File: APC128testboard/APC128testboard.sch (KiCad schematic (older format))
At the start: 2 parts, among them P1 CONN_20X2

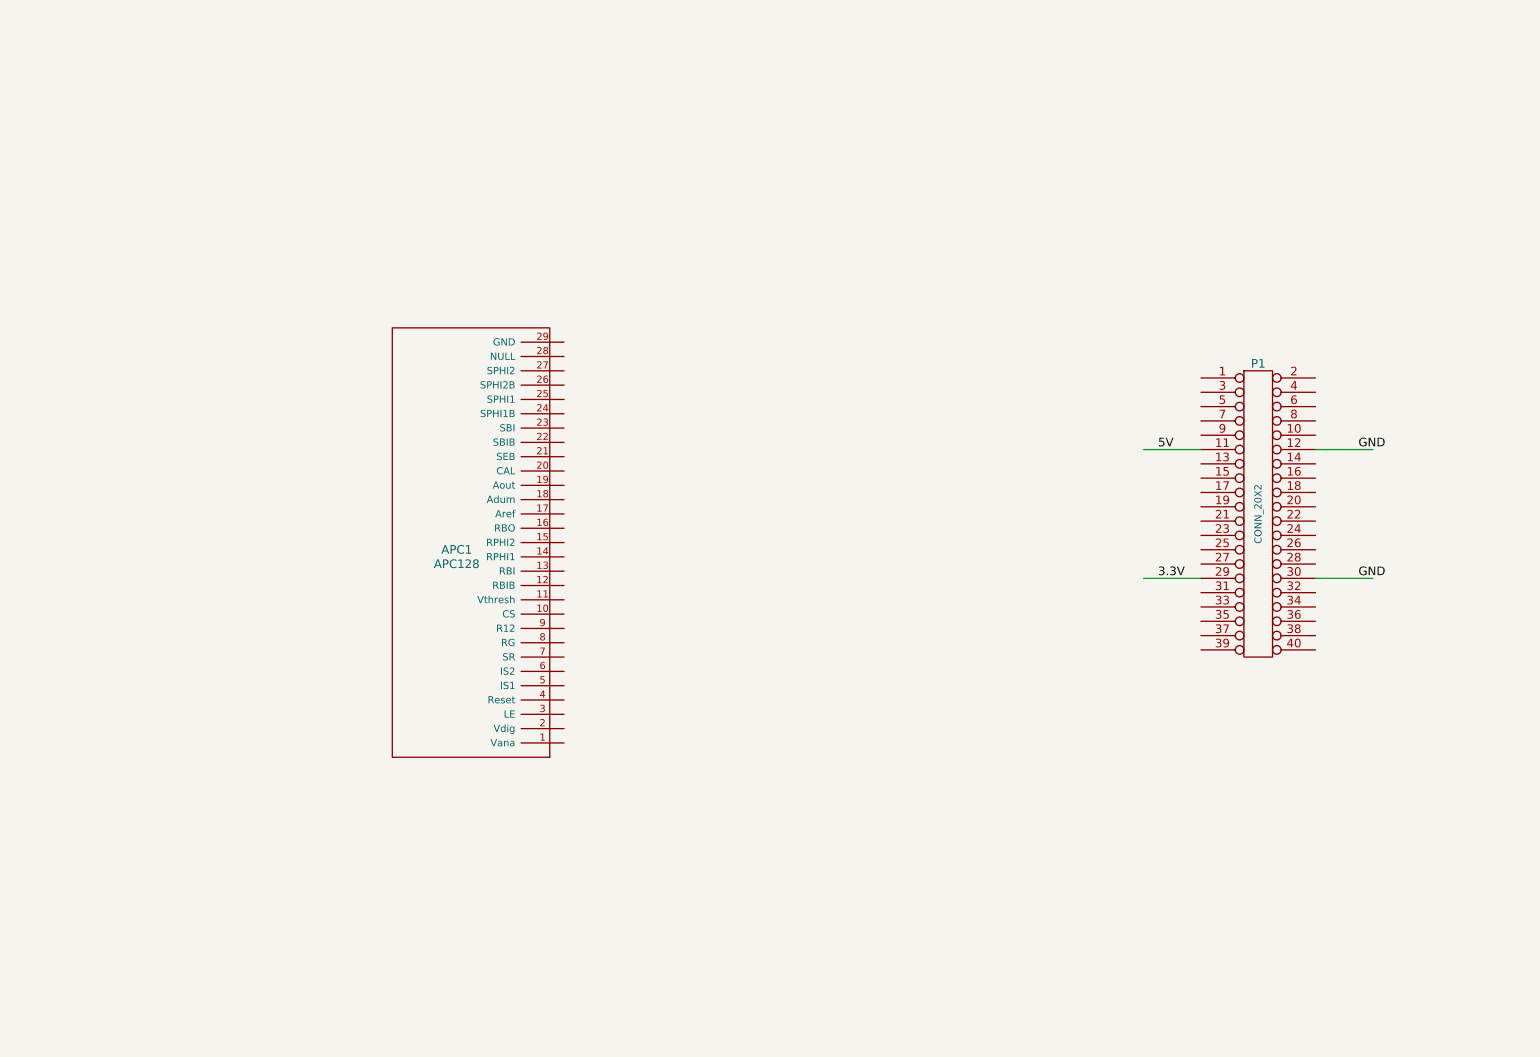
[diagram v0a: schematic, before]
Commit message: Moved existing Kicad files to legacy because they adhere to a depreciated version of Kicad. Added the APC128testboard project.
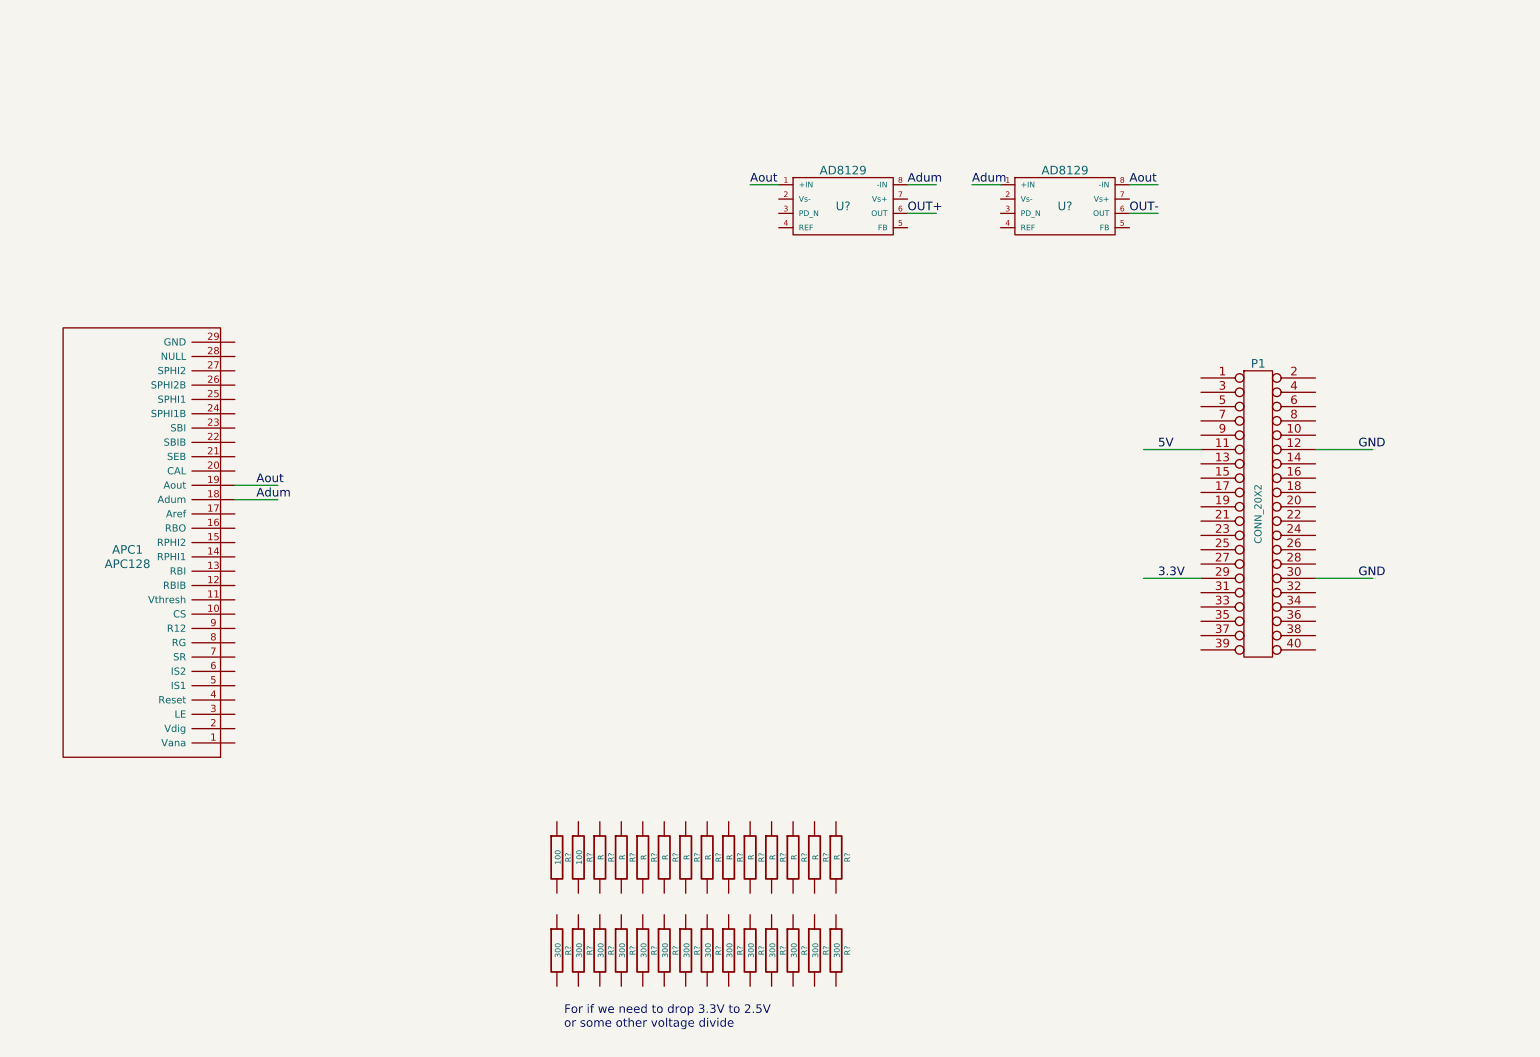
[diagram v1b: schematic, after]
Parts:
- added R? (x14): 300, symbol R
- added R? (x12): R, symbol R
- added R? (x2): 100, symbol R
- added U? (x2): AD8129, symbol AD8129
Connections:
- net labels added: Adum, Aout, OUT+, OUT-
- wire segments 4 -> 12
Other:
- note added: "For if we need to drop 3.3V to 2.5V \nor some other voltage divide"
- moved on the sheet: APC1

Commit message: Add DAC and pots to APC128testboard for adjustable analog inputs.
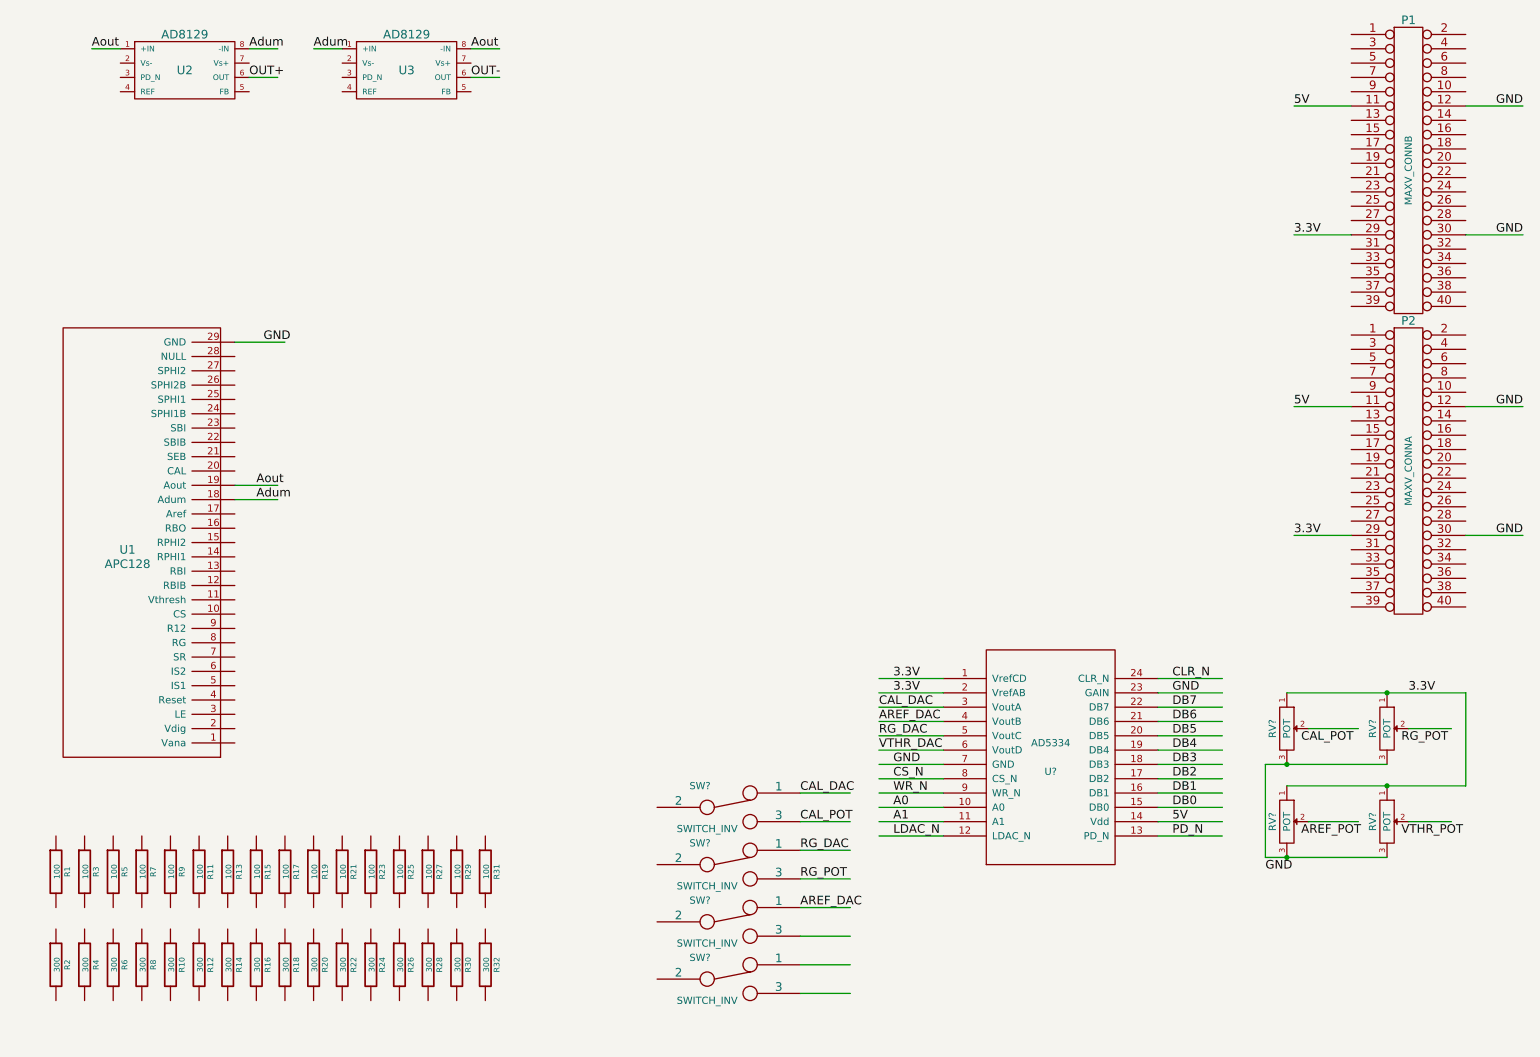
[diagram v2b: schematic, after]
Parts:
- removed R? (x13): 300, symbol R
- removed R? (x12): R, symbol R
- removed R?: 100, symbol R
- added P1: MAXV_CONNB, symbol CONN_20X2
- added R1, R11, R13, R15, R19, R21, R23, R25, R27, R29, R3, R31, R5, R7, R9: 100, symbol R
- added R10, R12, R14, R16, R2, R20, R22, R24, R26, R28, R30, R32, R4, R6, R8: 300, symbol R
- added RV? (x4): POT, symbol POT
- added SW? (x4): SWITCH_INV, symbol SWITCH_INV
- added U?: AD5334, MODULE, symbol AD5334
- P2: renamed from P1; value CONN_20X2 -> MAXV_CONNA
- gave numbers to parts that had none: 4
- renumbered APC1 to U1
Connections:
- net labels added: A0, A1, AREF_DAC, AREF_POT, CAL_DAC, CAL_POT, CLR_N, CS_N, DB0, DB1, DB2, DB3, DB4, DB5, DB6, DB7, LDAC_N, PD_N, RG_DAC, RG_POT, VTHR_DAC, VTHR_POT, WR_N
- wire segments 12 -> 59
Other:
- note removed: "For if we need to drop 3.3V to 2.5V \nor some other voltage divide"
- moved on the sheet: P2, R17, R18, U2, U3

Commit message: Continued progress on APC128Testboard.
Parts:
- R29, R31: value 100 -> R
- R30, R32: value 300 -> R
- gave numbers to parts that had none: 9
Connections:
- net labels added: AREF, CAL, CS, CS_d, IS1, IS1_d, IS2, IS2_d, LE, LE_d, R12, R12_d, RBI, RBI_d, RG, RPhi1, RPhi1_d, RPhi2, RPhi2_d, Reset, Reset_d, SBI, SBI_d, SEB, SEB_d, SPhi1, SPhi1_d, SPhi2, SPhi2_d, SR, SR_d, Sphi2_d, VTHR
- wire segments 59 -> 133
- no-connect marks 0 -> 5
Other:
- note added: "ConnA: 3.3V\nConnB: 2.5V"
- moved on the sheet: R10, R12, R14, R16, R18, R2, R20, R22, R24, R26, R28, R4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

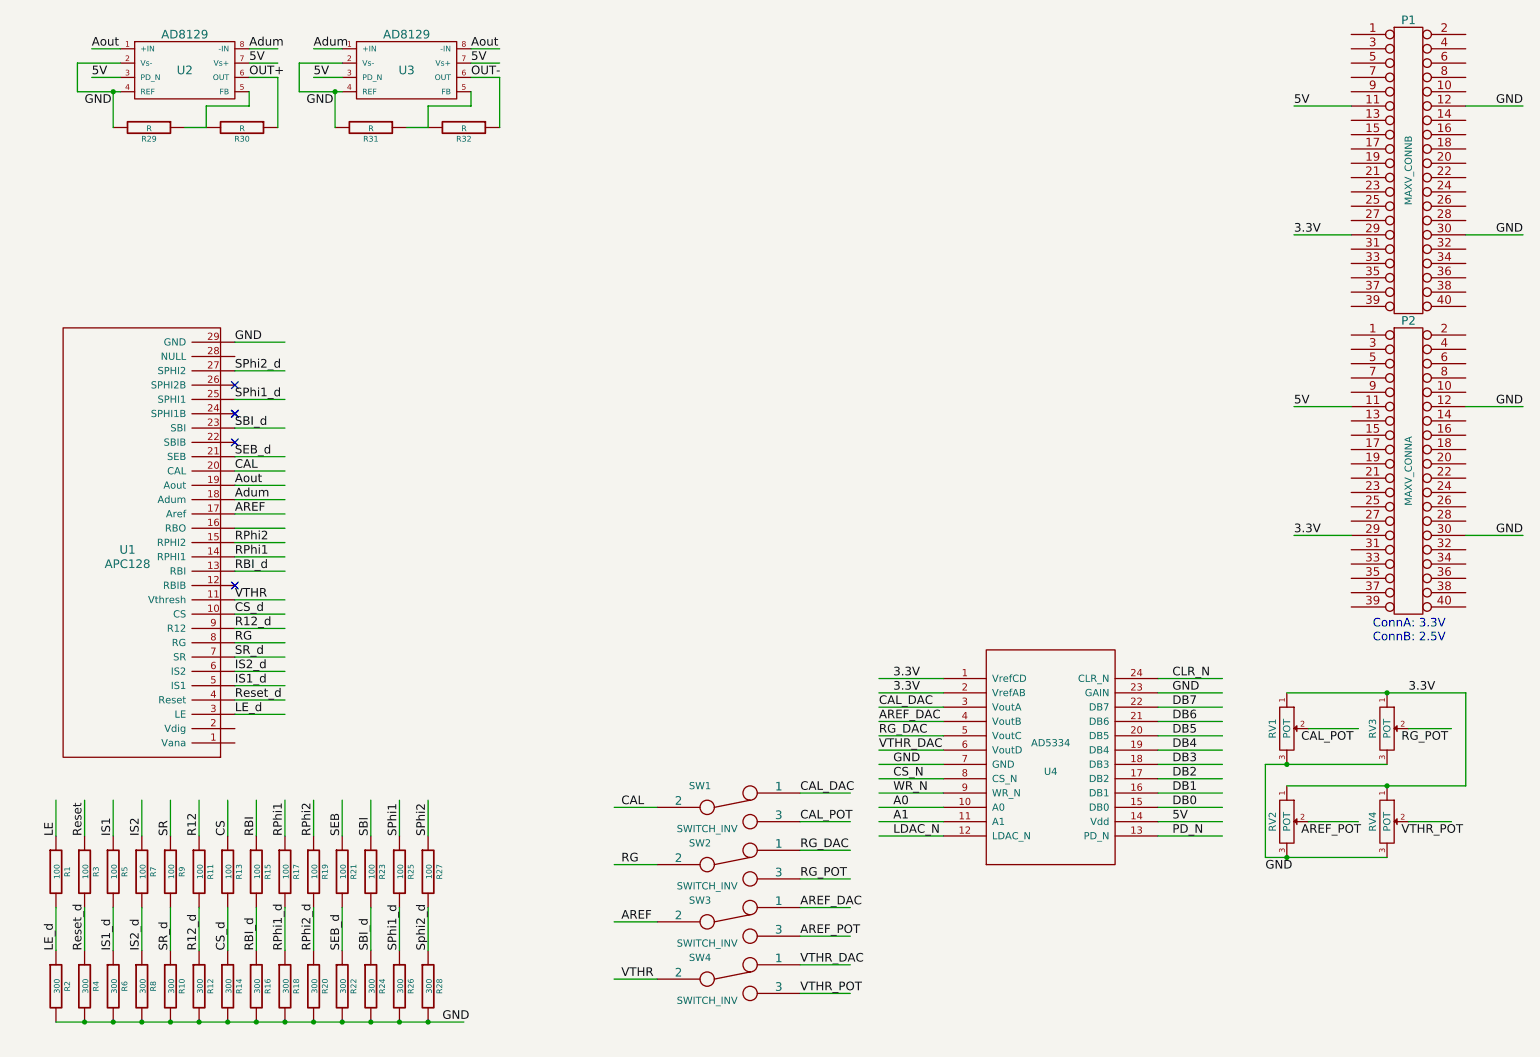
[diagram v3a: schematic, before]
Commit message: Finished first iteration of APC128Testboard circuit design.
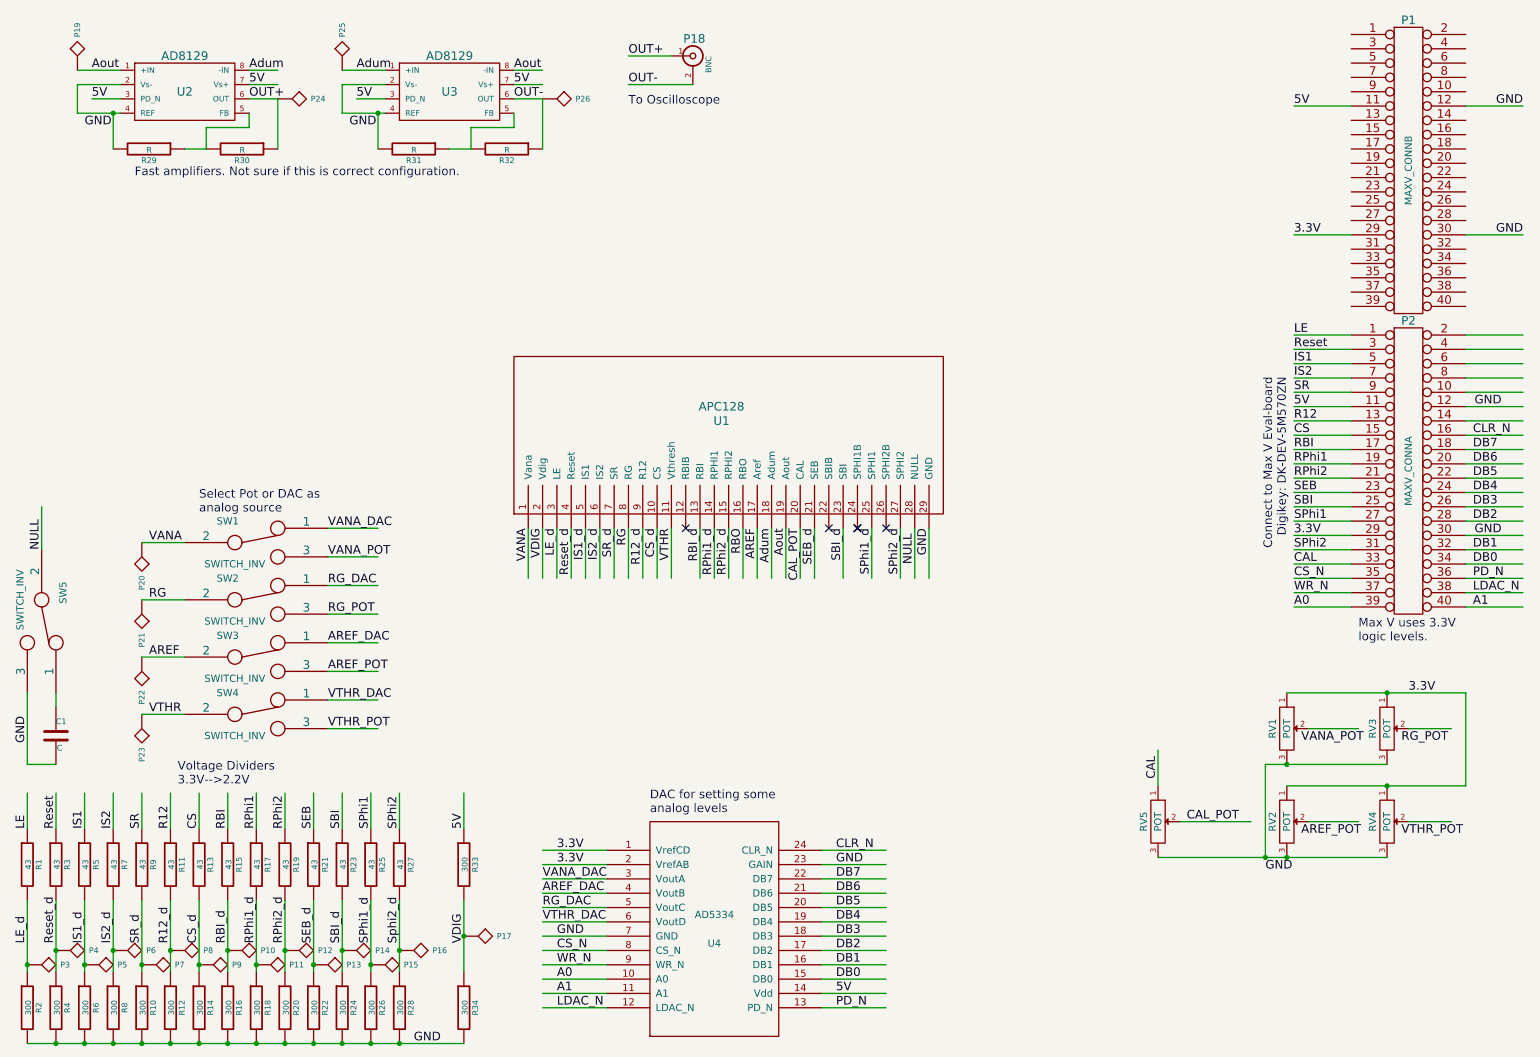
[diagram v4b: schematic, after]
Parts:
- added C1: C, symbol C
- added P10, P11, P12, P13, P14, P15, P16, P17, P19, P20, P21, P22, P23, P24, P25, P26, P3, P4, P5, P6, P7, P8, P9: SPYPAD, symbol SPYPAD
- added P18: BNC, symbol BNC
- added R33, R34: 300, symbol R
- added RV5: POT, symbol POT
- added SW5: SWITCH_INV, symbol SWITCH_INV
- R1, R11, R13, R15, R17, R19, R21, R23, R25, R27, R3, R5, R7, R9: value 100 -> 43
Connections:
- net labels added: NULL, RBO, VANA, VANA_DAC, VANA_POT, VDIG
- net labels removed: CAL_DAC
- wire segments 133 -> 182
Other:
- note added: "Connect to Max V Eval-board\nDigikey: DK-DEV-5M570ZN"
- note added: "DAC for setting some \nanalog levels"
- note added: "Fast amplifiers. Not sure if this is correct configuration."
- note added: "Max V uses 3.3V\nlogic levels."
- note added: "Select Pot or DAC as \nanalog source"
- note added: "To Oscilloscope"
- note added: "Voltage Dividers \n3.3V-->2.2V"
- note removed: "ConnA: 3.3V\nConnB: 2.5V"
- moved on the sheet: R1, R10, R11, R12, R13, R14, R15, R16, R17, R18, R19, R2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
